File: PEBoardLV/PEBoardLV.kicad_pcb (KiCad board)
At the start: 4 copper layers, 113.7 x 78.7 mm, 69 parts, among them J1 BSPD Test Jumper, J10 ECU Debug Connector, J11 SWD Header, J12 Extra Pin Header, J13 CAN Header, J14 UART Header, J15 To TSAL, J2 Beam Interlock, J3 To HV Interlocks, J4 To Left Panel, J5 To Right Panel, J6 To Brake Light, J7 To PE HV, J8 BSPD Reset, J9 Main LV Connector, U1 MCP6004, U10 ISO1050, U11 STM32F405, U2 4072, U3 4071, U4 DE1A1B-L2-12V, U5 74HC595, U6 LM555N, U7 SN754410, U8 NCP1117DT33RKG, U9 L78S05CV-DG, Y1 8MHz

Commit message: prepare to re-send PE LV board
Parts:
- C14, C15, C16, C17, C18, C19: footprint Capacitors_SMD:C_0603_HandSoldering -> FSFootprints:C_0402_HandSoldering
- U11: footprint Housings_QFP:LQFP-64_10x10mm_Pitch0.5mm -> FSFootprints:LQFP-64_10x10mm_Pitch0.5mm_HandSoldering
- moved C4 1.55 mm to (112.4, 78.7)
- moved C18 1.27 mm to (114.9, 60.3), turned to 90 degrees
- moved C17 0.90 mm to (118.7, 56.5)
- moved C12 0.90 mm to (126.4, 74.3)
- moved C14 0.90 mm to (128.3, 73.7), turned to 270 degrees
- moved U4 0.68 mm to (87.0, 94.0)
- moved R2 0.64 mm to (154.3, 78.7)
- moved R3 0.64 mm to (158.1, 78.7)
- moved R4 0.64 mm to (161.9, 78.7)
- moved R6 0.64 mm to (154.3, 66.0)
- moved C1 0.64 mm to (118.7, 83.8)
- moved C15 0.64 mm to (132.7, 60.3)
- moved U2 0.64 mm to (113.7, 88.9)
- moved U6 0.64 mm to (101.0, 74.9)
- moved U7 0.64 mm to (101.0, 86.4)
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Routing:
- net +12V: track 0.00 -> 224.7 mm
- net /STATUS_LED_3: track 0.00 -> 145.3 mm, vias 0 -> 1
- net /STATUS_LED_2: track 0.00 -> 127.0 mm, vias 0 -> 1
- net /AIRS_FINAL: track 0.00 -> 119.0 mm, vias 0 -> 1
- net /SIG_CURRENT: track 0.00 -> 118.7 mm
- net /AIRS_ACC_OUT: track 0.00 -> 94.9 mm
- net /LED_BSPD: track 0.00 -> 94.0 mm
- net /BUTTON_2: track 0.00 -> 93.5 mm, vias 0 -> 1
- net /SIG_BSE: track 0.00 -> 92.0 mm, vias 0 -> 2
- net /BSPD_RESET: track 0.00 -> 88.2 mm
- net +3V3: track 0.00 -> 86.4 mm, vias 0 -> 11
- net /BRAKELT_H: track 0.00 -> 83.4 mm
- net /BUTTON_1: track 0.00 -> 75.1 mm, vias 0 -> 2
- net /SIG_STEER: track 0.00 -> 74.4 mm
- net /SIG_APPS_A: track 0.00 -> 71.2 mm
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
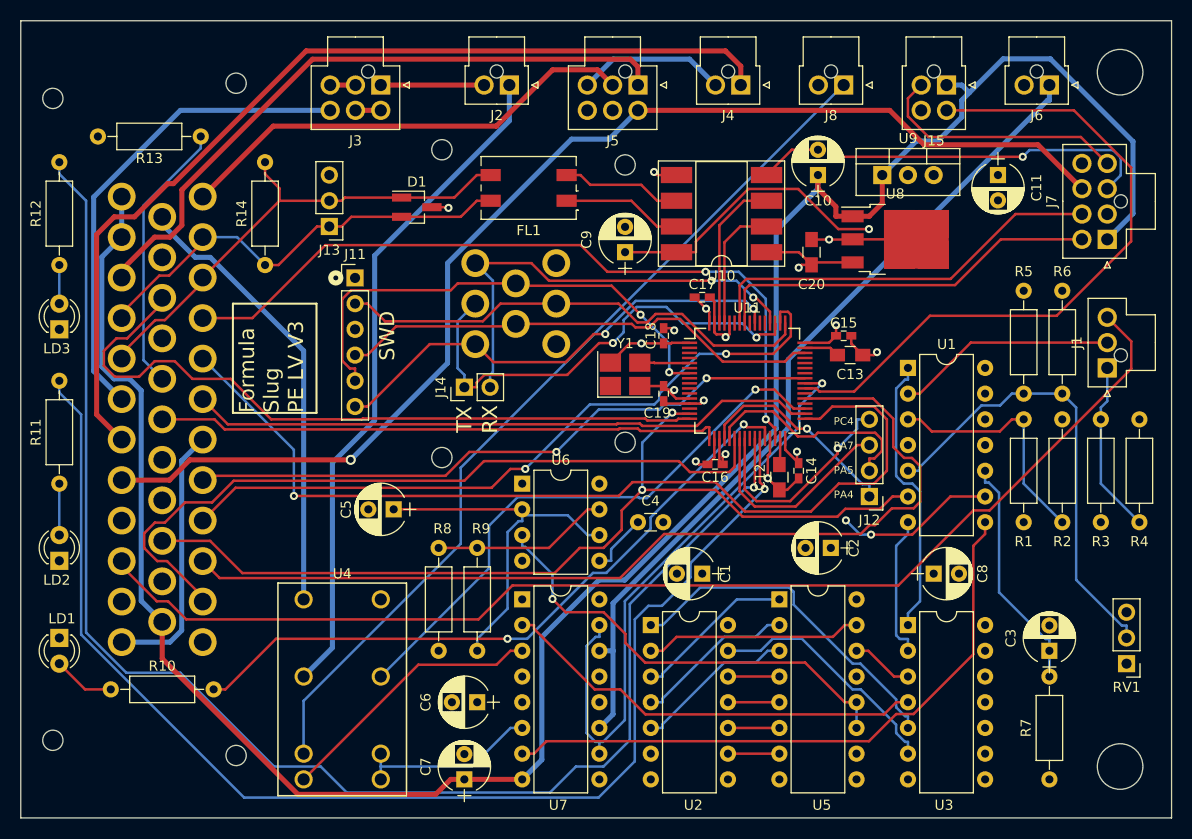
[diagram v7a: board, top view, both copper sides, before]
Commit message: Move LEDs on PE LV board
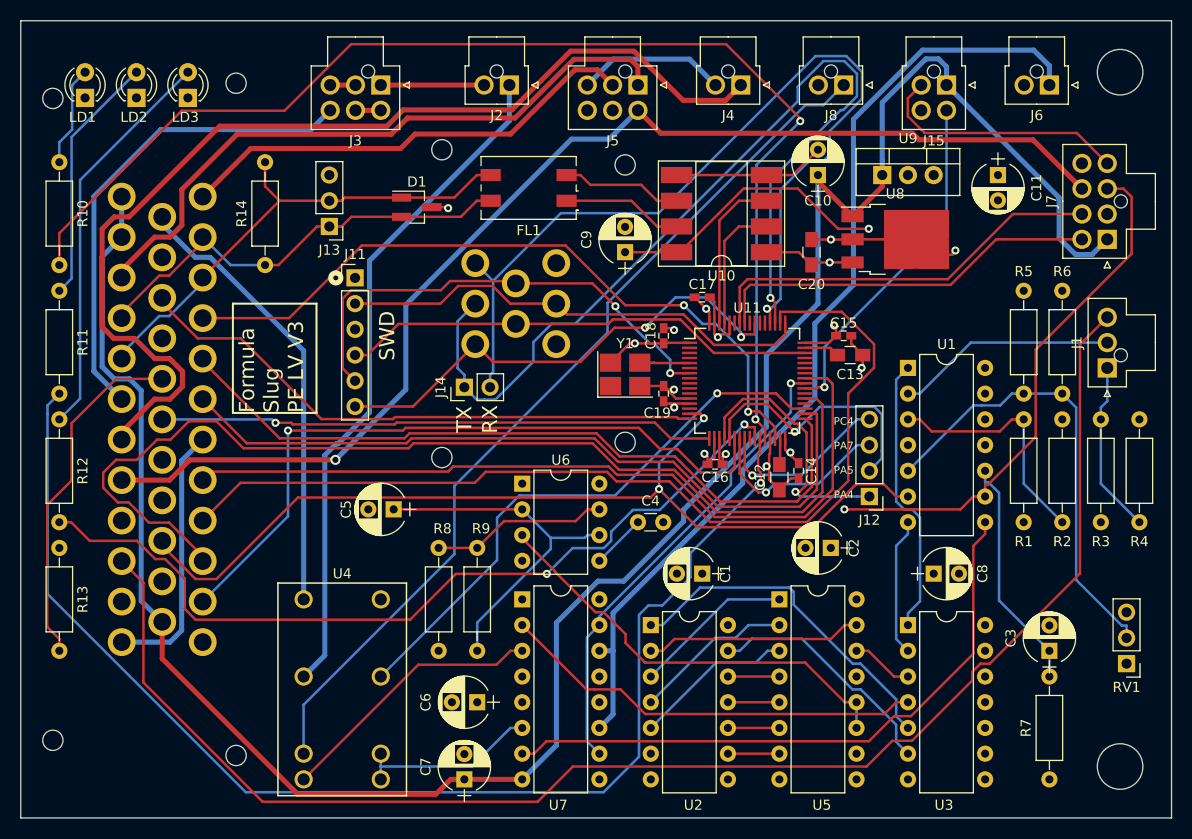
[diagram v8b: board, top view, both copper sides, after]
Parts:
- moved LD1 53.4 mm to (57.8, 36.8), turned to 90 degrees
- moved R10 52.3 mm to (55.2, 43.2), turned to 270 degrees
- moved LD2 46.4 mm to (62.9, 36.8)
- moved R13 40.8 mm to (55.2, 81.3), turned to 270 degrees
- moved LD3 26.2 mm to (67.9, 36.8)
- moved R11 19.1 mm to (55.2, 55.9), turned to 270 degrees
- moved R12 15.2 mm to (55.2, 68.6), turned to 270 degrees
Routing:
- net /STATUS_LED_3: track 145.3 -> 84.2 mm, vias 1 -> 2
- net /STATUS_LED_1: track 67.2 -> 121.0 mm
- net /UART_TX: track 46.7 -> 93.4 mm, vias 2 -> 1
- net /UART_RX: track 45.3 -> 89.3 mm, vias 2 -> 1
- net Net-(LD3-Pad2): track 3.81 -> 39.6 mm
- net /SIG_RTDS: track 66.4 -> 34.3 mm, vias 0 -> 1
- net /SIG_CURRENT: track 118.7 -> 146.5 mm
- net /LED_IMD: track 70.4 -> 95.8 mm, vias 2 -> 0
- net Net-(LD2-Pad2): track 5.08 -> 24.7 mm
- net /BUTTON_2: track 93.5 -> 74.2 mm, vias 1 -> 0
- net /LED_AMS: track 63.7 -> 79.4 mm, vias 2 -> 0
- net /SIG_BRAKELT: track 60.6 -> 46.8 mm
- net /SIG_APPS_A: track 71.2 -> 57.5 mm
- net /BRAKELT_H: track 83.4 -> 96.6 mm
- net /BUTTON_3: track 62.2 -> 74.8 mm
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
